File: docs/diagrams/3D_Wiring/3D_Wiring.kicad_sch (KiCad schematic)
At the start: 21 parts, among them J1 USB to Power, J2 USB to Computer, M1 Stepper_Motor, Q1 TIP120, Q2 TIP120, Q3 TIP120, Q4 TIP120, U1 ULN2003, U2 MT3608

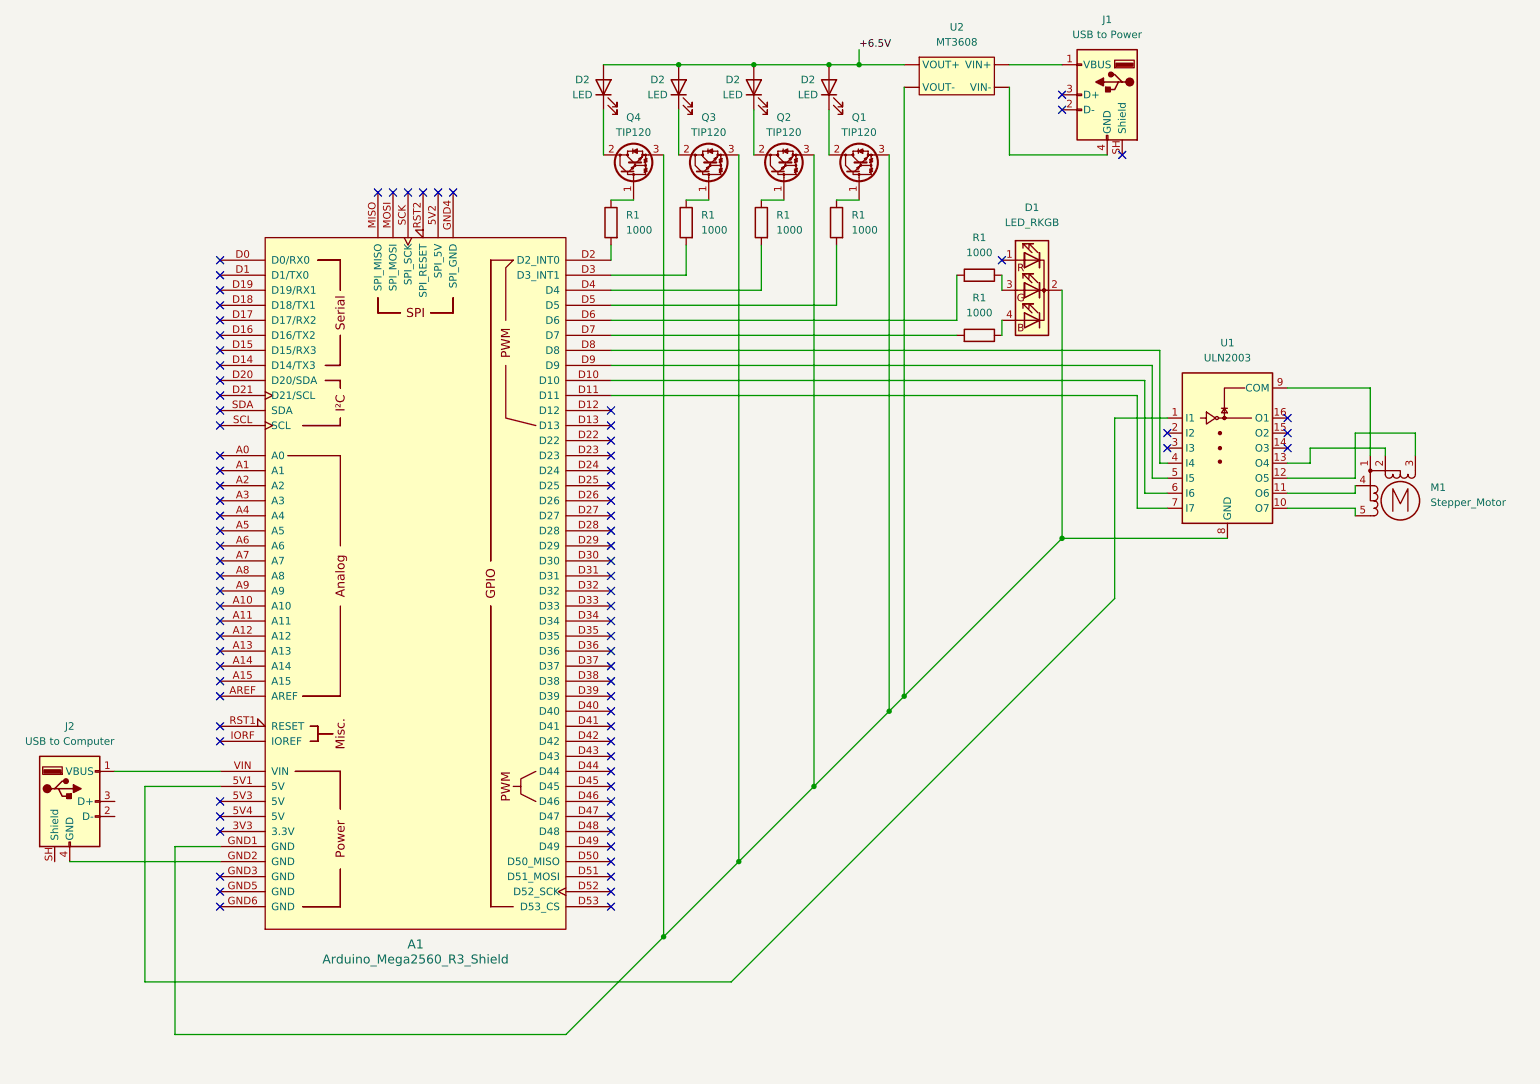
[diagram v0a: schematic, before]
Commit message: Updated 2D wiring diagram, added 3D wiring diagram
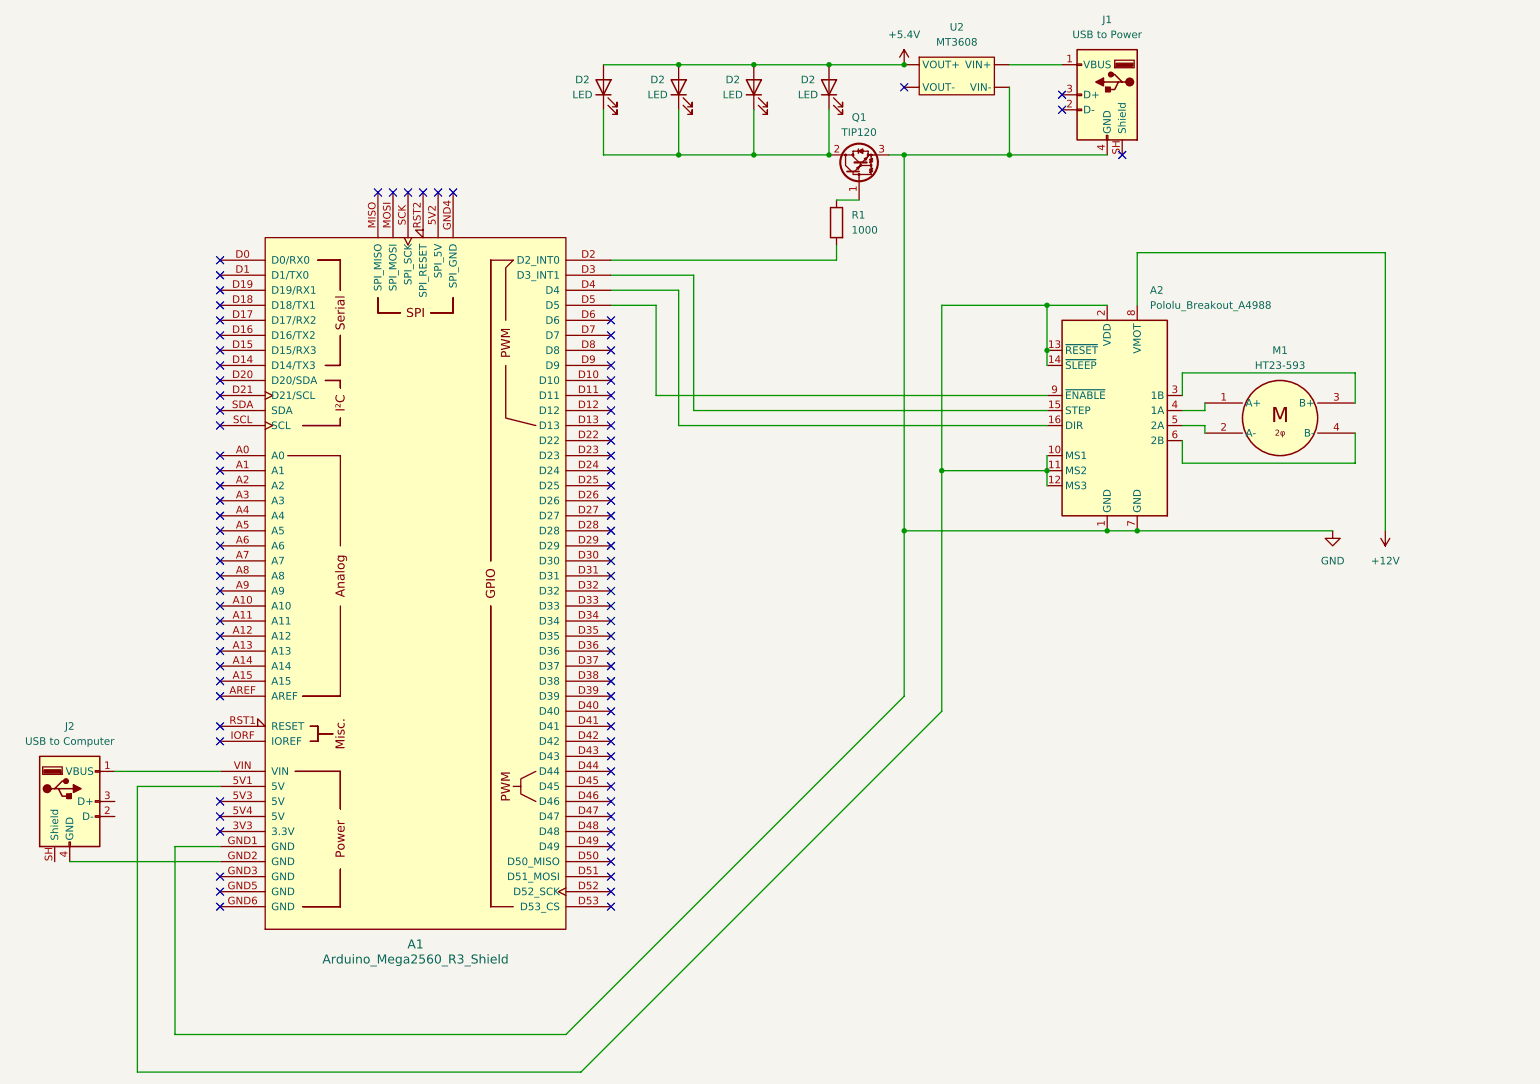
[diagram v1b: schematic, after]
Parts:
- removed D1: LED_RKGB, symbol Device:LED_RKGB
- removed M1: Stepper_Motor, symbol Motor:Stepper_Motor_unipolar_5pin
- removed Q2, Q3, Q4: TIP120, Package_TO_SOT_THT:TO-220-3_Vertical, symbol Transistor_BJT:TIP120
- removed R1 (x5): 1000, symbol Device:R
- removed U1: ULN2003, symbol Transistor_Array:ULN2003
- added A2: Pololu_Breakout_A4988, Module:Pololu_Breakout-16_15.2x20.3mm, symbol Driver_Motor:Pololu_Breakout_A4988
- added M1: HT23-593, symbol HT23-593:HT23-593
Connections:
- net GND: now reaches A1.GND1 (GND), Q1.3 (E), U2. (VIN-)
- net GND: now also J1.4 (GND), A2.1 (GND), A2.7 (GND)
- net at D2.1 (K): now also D2.1 (K), D2.1 (K), D2.1 (K), Q1.2 (C)
- net at A1.D3 (D3_INT1): now also A2.15 (STEP)
- net at A1.D2 (D2_INT0): now also R1.2
- net at A1.5V1 (5V): now also A2.10 (MS1), A2.11 (MS2), A2.12 (MS3), A2.13 (~{RESET}), A2.14 (~{SLEEP}), A2.2 (VDD)
- net at A1.D4: now also A2.16 (DIR)
- net at A1.D5: now also A2.9 (~{ENABLE}); no longer R1.2
- net +6.5V renamed +5.4V
- new net: A2.4 (1A), M1.1 (A+)
- new net: A2.5 (2A), M1.2 (A-)
- new net: A2.3 (1B), M1.3 (B+)
- new net: A2.6 (2B), M1.4 (B-)
- new net +12V: A2.8 (VMOT)
- no-connect marks 86 -> 87
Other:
- title: 2D System Wiring Diagram -> 3D System Wiring Diagram
